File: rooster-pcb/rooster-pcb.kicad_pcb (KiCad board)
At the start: 2 copper layers, 228 x 72 mm, 95 parts, among them SW0-0 SW_Push, SW0-1 SW_Push, SW0-10 SW_Push, SW0-11 SW_Push, SW0-2 SW_Push, SW0-3 SW_Push, SW0-4 SW_Push, SW0-5 SW_Push, SW0-6 SW_Push, SW0-7 SW_Push, SW0-8 SW_Push, SW0-9 SW_Push, SW1-0 SW_Push, SW1-1 SW_Push, SW1-10 SW_Push, SW1-11 SW_Push, SW1-2 SW_Push, SW1-3 SW_Push, SW1-4 SW_Push, SW1-5 SW_Push, SW1-6 SW_Push, SW1-7 SW_Push, SW1-8 SW_Push, SW1-9 SW_Push, SW2-0 SW_Push, SW2-1 SW_Push, SW2-10 SW_Push, SW2-11 SW_Push, SW2-2 SW_Push, SW2-3 SW_Push, SW2-4 SW_Push, SW2-5 SW_Push, SW2-6 SW_Push, SW2-7 SW_Push, SW2-8 SW_Push, SW2-9 SW_Push, SW3-0 SW_Push, SW3-1 SW_Push, SW3-10 SW_Push, SW3-11 SW_Push, SW3-2 SW_Push, SW3-3 SW_Push, SW3-4 SW_Push, SW3-5 SW_Push, SW3-7 SW_Push, SW3-8 SW_Push, SW3-9 SW_Push, U1 Sparkfun_Pro_Micro

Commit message: Replaced ProMicro symbol & footprint; adding mounting holes
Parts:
- added M1: MountingHole_2.2mm_M2_Pad_Via, MountingHole:MountingHole_2.2mm_M2_Pad_Via, F.Cu at (39.5, 39.0)
- added M2: MountingHole_2.2mm_M2_Pad_Via, MountingHole:MountingHole_2.2mm_M2_Pad_Via, F.Cu at (39.5, 75.0)
- added REF**: MountingHole_2.2mm_M2_Pad_Via, MountingHole:MountingHole_2.2mm_M2_Pad_Via, F.Cu at (229.5, 39.0)
- added REF**: MountingHole_2.2mm_M2_Pad_Via, MountingHole:MountingHole_2.2mm_M2_Pad_Via, F.Cu at (229.5, 75.0)
- U1: value Sparkfun_Pro_Micro -> ProMicro; footprint Arduino:Sparkfun_Pro_Micro -> Keyboard_Components:ArduinoProMicro
- moved U1 32.5 mm to (68.0, 40.2), turned to 270 degrees
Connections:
- SW0-10 pad 2: COLA -> COL10
- SW0-11 pad 2: COLB -> COL11
- SW1-10 pad 2: COLA -> COL10
- SW1-11 pad 2: COLB -> COL11
- SW2-10 pad 2: COLA -> COL10
- SW2-11 pad 2: COLB -> COL11
- SW3-10 pad 2: COLA -> COL10
- SW3-11 pad 2: COLB -> COL11
- U1 pad 1: COL1 -> Net-(U1-Pad1)
- U1 pad 10: COL7 -> ROW1
- U1 pad 11: COL8 -> ROW2
- U1 pad 12: COL9 -> ROW3
- U1 pad 13: COLA -> COL4
- U1 pad 14: COLB -> COL5
- U1 pad 15: ROW0 -> COL6
- U1 pad 16: ROW1 -> COL7
- U1 pad 17: ROW2 -> COL8
- U1 pad 18: ROW3 -> COL9
- U1 pad 19: Net-(U1-Pad19) -> COL10
- U1 pad 2: COL0 -> Net-(U1-Pad2)
- U1 pad 20: Net-(U1-Pad20) -> COL11
- U1 pad 5: COL2 -> COL0
- U1 pad 6: COL3 -> COL1
- U1 pad 7: COL4 -> COL2
- U1 pad 8: COL5 -> COL3
- U1 pad 9: COL6 -> ROW0

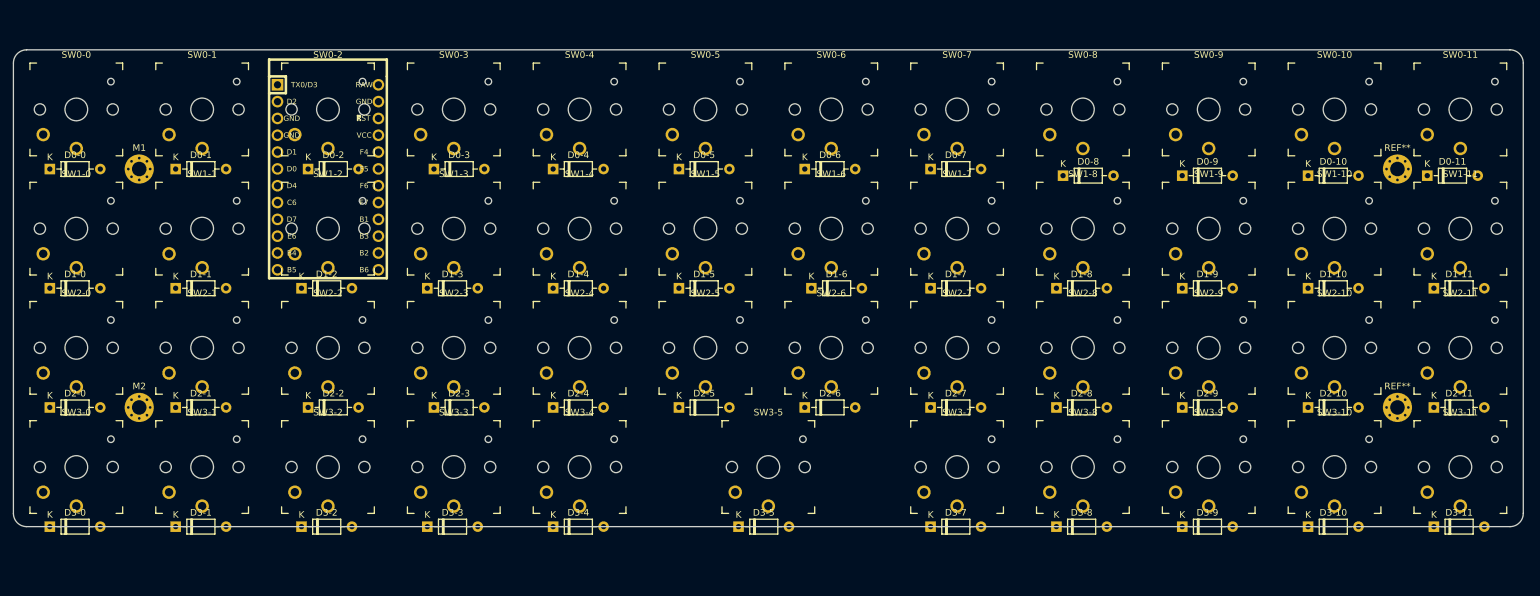
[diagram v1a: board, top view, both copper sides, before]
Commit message: Positioned diodes
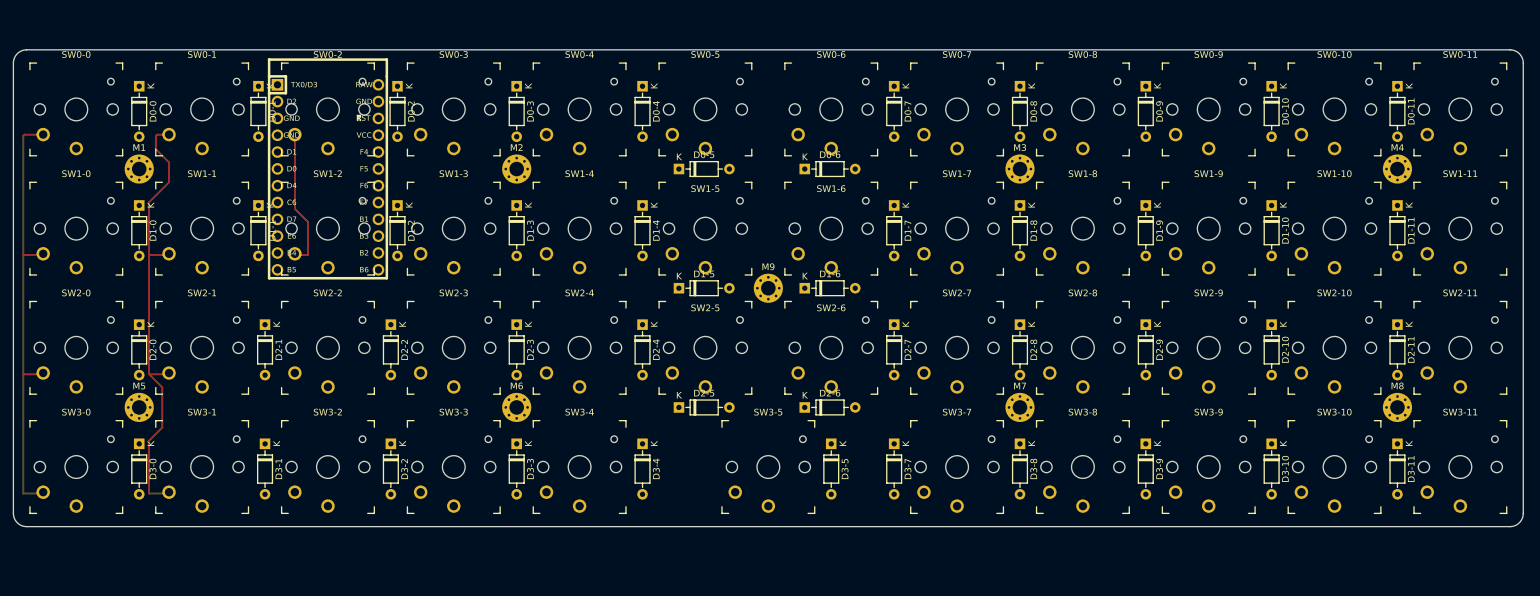
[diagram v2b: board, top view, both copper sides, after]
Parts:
- added M2: MountingHole_2.2mm_M2_Pad_Via, MountingHole:MountingHole_2.2mm_M2_Pad_Via, F.Cu at (96.5, 39.0)
- added M3: MountingHole_2.2mm_M2_Pad_Via, MountingHole:MountingHole_2.2mm_M2_Pad_Via, F.Cu at (172.5, 39.0)
- added M6: MountingHole_2.2mm_M2_Pad_Via, MountingHole:MountingHole_2.2mm_M2_Pad_Via, F.Cu at (96.5, 75.0)
- added M7: MountingHole_2.2mm_M2_Pad_Via, MountingHole:MountingHole_2.2mm_M2_Pad_Via, F.Cu at (172.5, 75.0)
- added M9: MountingHole_2.2mm_M2_Pad_Via, MountingHole:MountingHole_2.2mm_M2_Pad_Via, F.Cu at (134.5, 57.0)
- moved D1-2 19.1 mm to (78.5, 44.5), turned to 270 degrees
- moved D3-5 18.8 mm to (144.0, 80.5), turned to 270 degrees
- moved D0-0 18.4 mm to (39.5, 26.5), turned to 270 degrees
- moved D0-2 18.4 mm to (78.5, 26.5), turned to 270 degrees
- moved D0-4 18.4 mm to (115.5, 26.5), turned to 270 degrees
- moved D1-0 18.4 mm to (39.5, 44.5), turned to 270 degrees
- moved D1-3 18.4 mm to (96.5, 44.5), turned to 270 degrees
- moved D1-4 18.4 mm to (115.5, 44.5), turned to 270 degrees
- moved D2-0 18.4 mm to (39.5, 62.5), turned to 270 degrees
- moved D2-1 18.4 mm to (58.5, 62.5), turned to 270 degrees
- moved D2-4 18.4 mm to (115.5, 62.5), turned to 270 degrees
- moved D3-0 18.4 mm to (39.5, 80.5), turned to 270 degrees
- moved D3-1 18.4 mm to (58.5, 80.5), turned to 270 degrees
- moved D3-2 18.4 mm to (77.5, 80.5), turned to 270 degrees
- moved D3-3 18.4 mm to (96.5, 80.5), turned to 270 degrees
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- renumbered REF** to M4, M2 to M5, REF** to M8
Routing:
- net COL1: track 0.00 -> 69.1 mm
- net COL0: track 0.00 -> 66.3 mm
- net COL2: track 0.00 -> 21.1 mm

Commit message: Flipped diodes to back side; started tracing columns
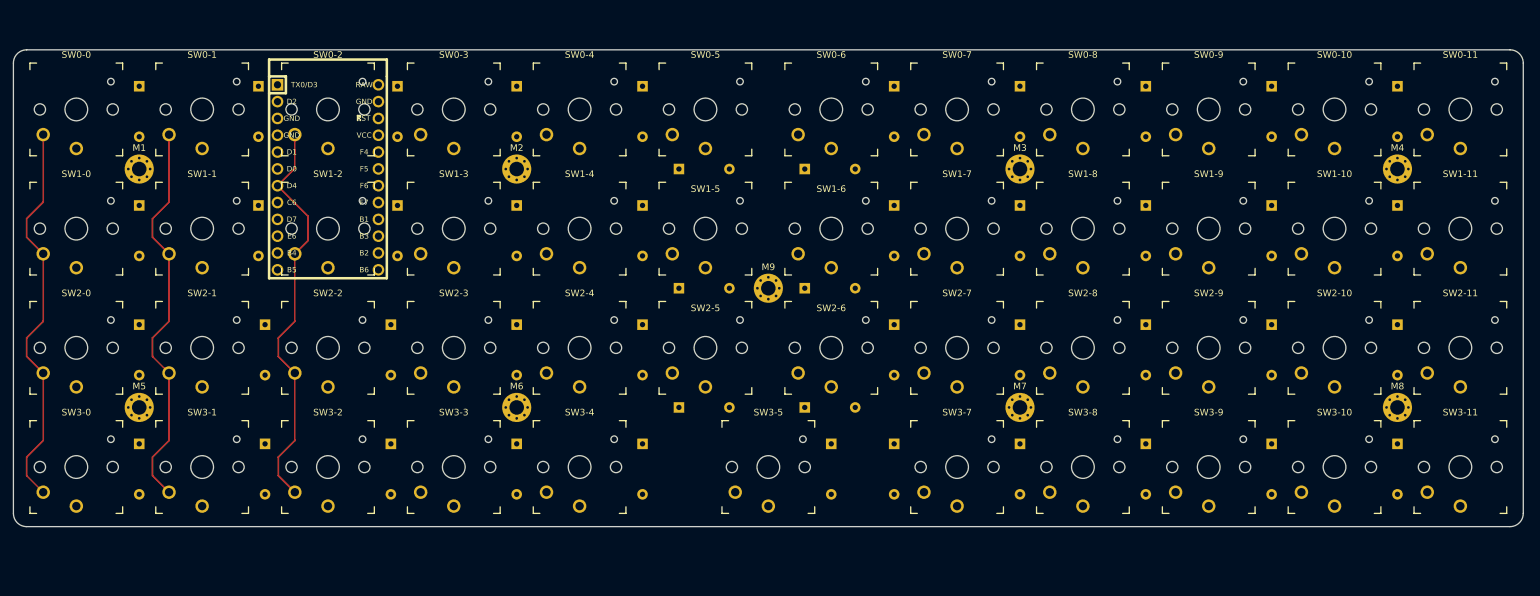
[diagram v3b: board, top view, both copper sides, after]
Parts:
- D0-0, D0-1, D0-10, D0-11, D0-2, D0-3, D0-4, D0-5, D0-6, D0-7, D0-8, D0-9, D1-0, D1-1, D1-10, D1-11, D1-2, D1-3, D1-4, D1-5, D1-6, D1-7, D1-8, D1-9, D2-0, D2-1, D2-10, D2-11, D2-2, D2-3, D2-4, D2-5, D2-6, D2-7, D2-8, D2-9, D3-0, D3-1, D3-10, D3-11, D3-2, D3-3, D3-4, D3-5, D3-7, D3-8, D3-9: moved to B.Cu
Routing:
- net COL2: track 21.1 -> 62.3 mm
- net COL1: track 69.1 -> 61.1 mm
- net COL0: track 66.3 -> 61.1 mm

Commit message: Adding horizontal traces
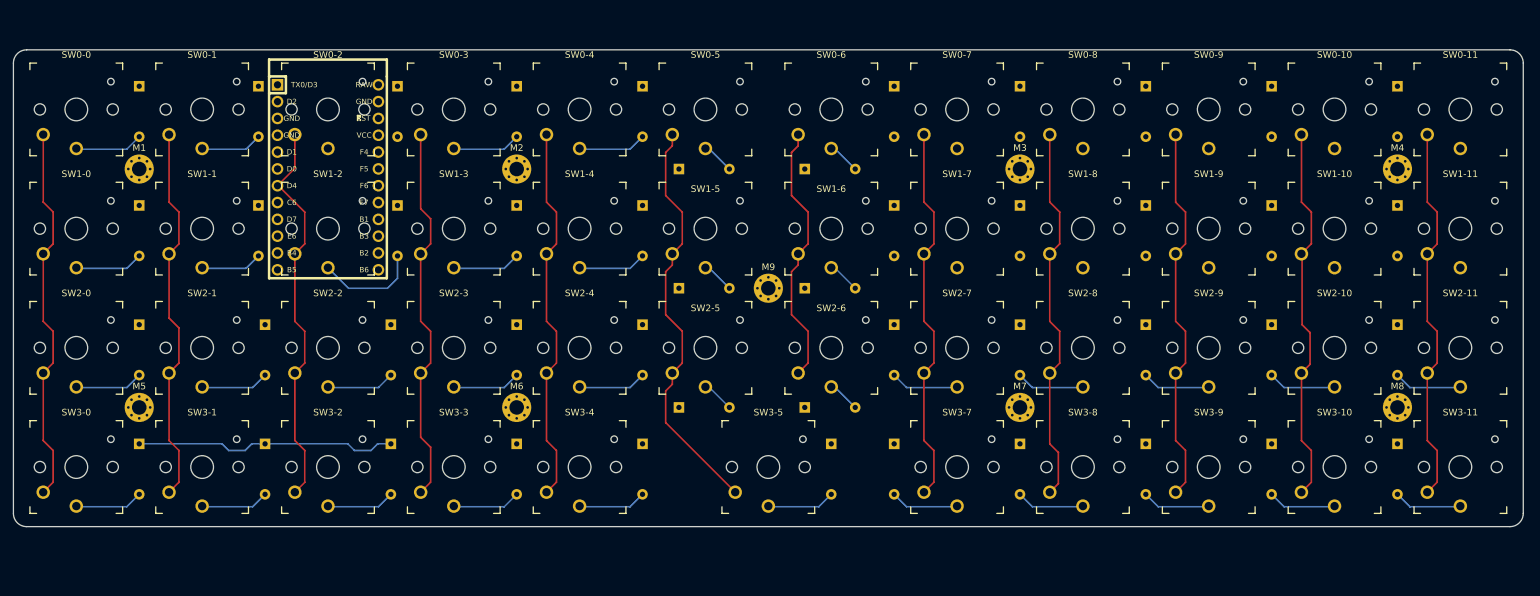
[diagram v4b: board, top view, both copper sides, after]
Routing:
- net COL5: track 0.00 -> 62.9 mm
- net COL9: track 0.00 -> 57.7 mm
- net COL7: track 0.00 -> 57.7 mm
- net COL4: track 0.00 -> 57.7 mm
- net COL3: track 0.00 -> 57.7 mm
- net COL11: track 0.00 -> 57.7 mm
- net COL8: track 0.00 -> 57.6 mm
- net COL10: track 0.00 -> 57.6 mm
- net COL6: track 0.00 -> 40.1 mm
- net ROW3: track 0.00 -> 39.7 mm
- net Net-(D1-2-Pad2): track 0.00 -> 15.8 mm
- net Net-(D1-4-Pad2): track 0.00 -> 10.3 mm
- net Net-(D1-3-Pad2): track 0.00 -> 10.3 mm
- net Net-(D0-4-Pad2): track 0.00 -> 10.3 mm
- net Net-(D0-3-Pad2): track 0.00 -> 10.3 mm
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
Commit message: Finished routing; design rules passed
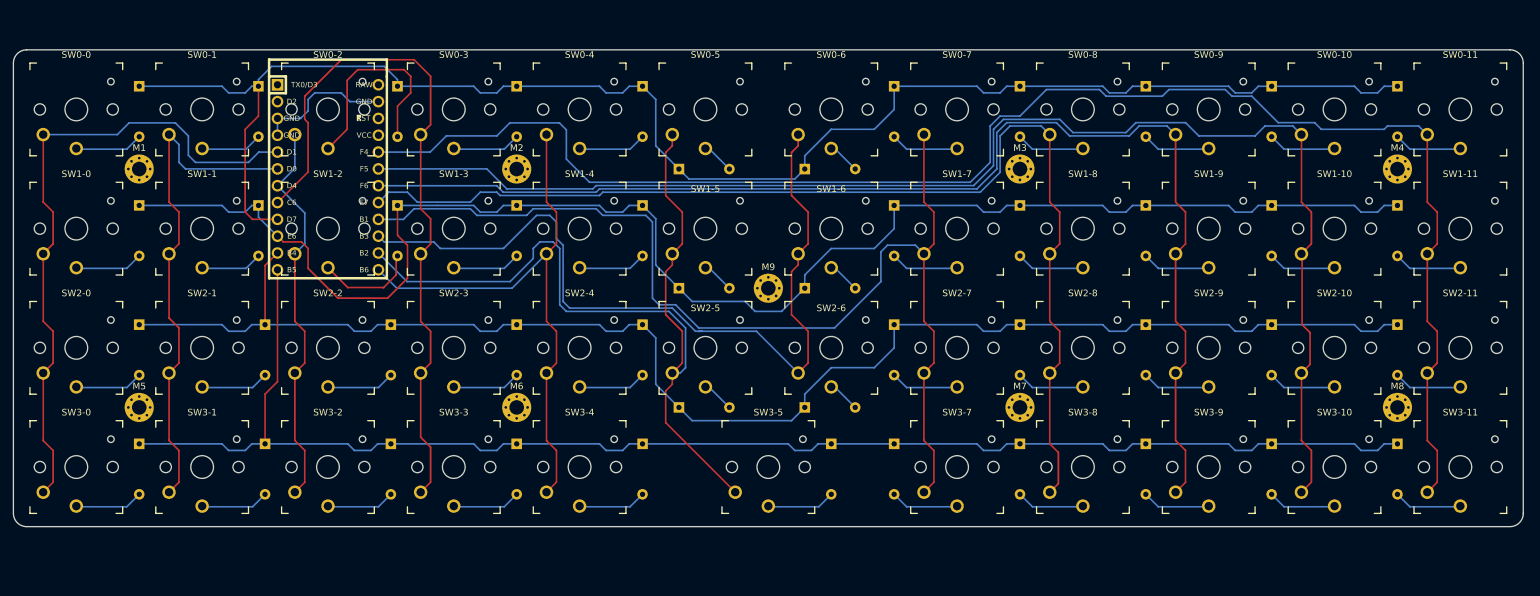
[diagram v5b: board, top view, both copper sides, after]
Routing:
- net ROW0: track 0.00 -> 244.5 mm
- net ROW1: track 0.00 -> 239.3 mm
- net ROW2: track 0.00 -> 227.6 mm
- net ROW3: track 39.7 -> 224.5 mm
- net COL11: track 57.7 -> 237.3 mm
- net COL10: track 57.6 -> 209.2 mm
- net COL9: track 57.7 -> 188.1 mm
- net COL8: track 57.6 -> 169.1 mm
- net COL7: track 57.7 -> 164.1 mm
- net COL6: track 40.1 -> 123.3 mm
- net COL5: track 62.9 -> 133.1 mm
- net COL3: track 57.7 -> 107.6 mm
- net COL0: track 58.6 -> 99.5 mm
- net Net-(D0-2-Pad2): track 0.00 -> 32.1 mm
- net COL4: track 57.7 -> 86.4 mm
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
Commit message: Remade PCB for 0.5mm spacing between keycaps + surface-mounted diodes
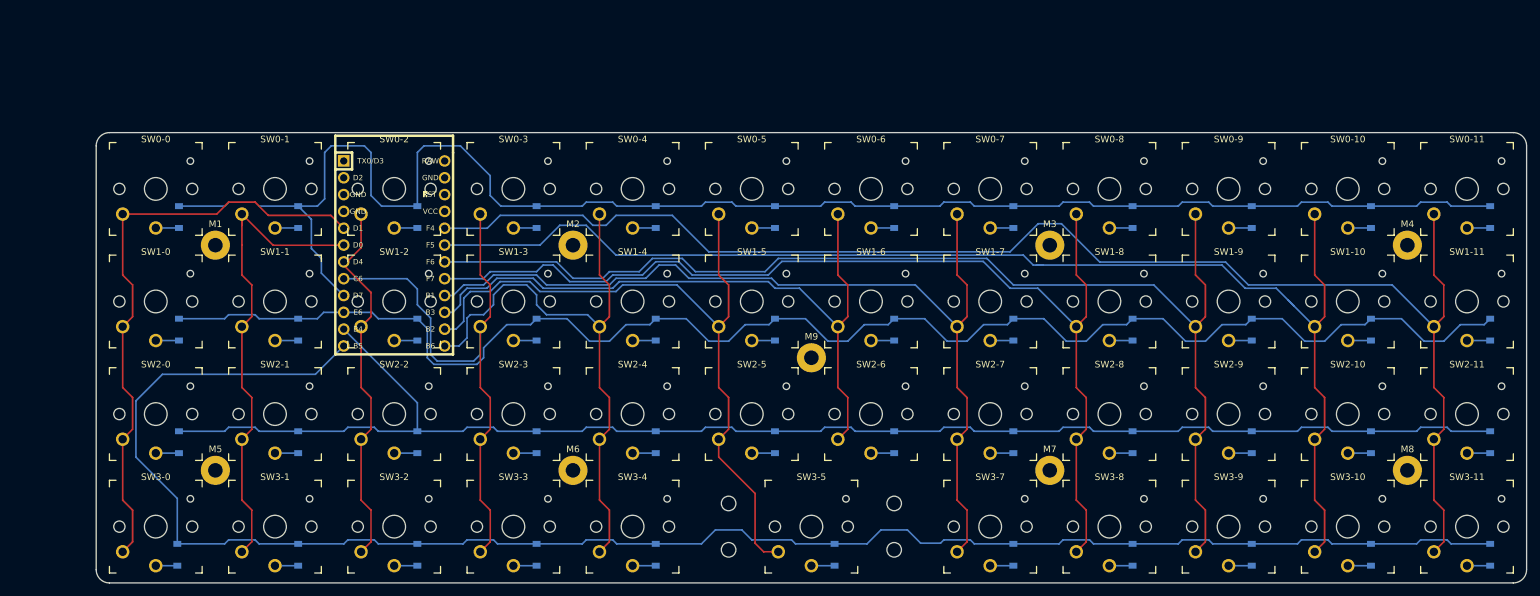
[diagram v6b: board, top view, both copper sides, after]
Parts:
- added N1: MountingHole_2.2mm_M2, MountingHole:MountingHole_2.2mm_M2, F.Cu at (128.5, 89.5)
- added N2: MountingHole_2.2mm_M2, MountingHole:MountingHole_2.2mm_M2, F.Cu at (153.5, 89.5)
- added N3: MountingHole_2.2mm_M2, MountingHole:MountingHole_2.2mm_M2, F.Cu at (128.5, 96.5)
- added N4: MountingHole_2.2mm_M2, MountingHole:MountingHole_2.2mm_M2, F.Cu at (153.5, 96.5)
- D0-0, D0-1, D0-10, D0-11, D0-2, D0-3, D0-4, D0-5, D0-6, D0-7, D0-8, D0-9, D1-0, D1-1, D1-10, D1-11, D1-2, D1-3, D1-4, D1-5, D1-6, D1-7, D1-8, D1-9, D2-0, D2-1, D2-10, D2-11, D2-2, D2-3, D2-4, D2-5, D2-6, D2-7, D2-8, D2-9, D3-0, D3-1, D3-10, D3-11, D3-2, D3-3, D3-4, D3-5, D3-7, D3-8, D3-9: footprint Diode_THT:D_DO-35_SOD27_P7.62mm_Horizontal -> Diode_SMD:D_SOD-123
- M1, M2, M3, M4, M5, M6, M7, M8, M9: value MountingHole_2.2mm_M2_Pad_Via -> MountingHole_2.2mm_M2_Pad; footprint MountingHole:MountingHole_2.2mm_M2_Pad_Via -> MountingHole:MountingHole_2.2mm_M2_Pad
- moved D0-7 26.7 mm to (171.5, 46.2)
- moved D0-8 26.1 mm to (189.5, 46.2)
- moved D1-7 26.0 mm to (171.5, 63.2)
- moved D0-9 25.4 mm to (207.5, 46.2)
- moved D1-8 25.3 mm to (189.5, 63.2)
- moved D2-7 25.3 mm to (171.5, 80.2)
- moved D0-10 24.8 mm to (225.5, 46.2)
- moved D1-9 24.6 mm to (207.5, 63.2)
- moved D3-7 24.6 mm to (171.5, 97.2)
- moved D2-8 24.6 mm to (189.5, 80.2)
- moved D0-11 24.2 mm to (243.5, 46.2)
- moved D1-10 24.0 mm to (225.5, 63.2)
- moved D2-9 23.9 mm to (207.5, 80.2)
- moved D3-8 23.9 mm to (189.5, 97.2)
- moved D1-11 23.4 mm to (243.5, 63.2)
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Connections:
- U1 pad 3: GND -> Net-(U1-Pad3)
- U1 pad 4: GND -> Net-(U1-Pad4)
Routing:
- net ROW3: track 224.5 -> 265.1 mm
- net Net-(D0-2-Pad2): track 32.1 -> 3.50 mm
- net COL7: track 164.1 -> 139.1 mm
- net COL5: track 133.1 -> 108.6 mm
- net GND: track 20.9 -> 0.00 mm
- net COL11: track 237.3 -> 216.6 mm
- net COL6: track 123.3 -> 102.7 mm
- net COL3: track 107.6 -> 89.7 mm
- net COL10: track 209.2 -> 195.9 mm
- net Net-(D1-2-Pad2): track 15.3 -> 3.50 mm
- net COL9: track 188.1 -> 176.3 mm
- net COL8: track 169.1 -> 159.0 mm
- net COL0: track 99.5 -> 90.5 mm
- net ROW1: track 239.3 -> 231.0 mm
- net Net-(D3-0-Pad2): track 10.3 -> 3.25 mm
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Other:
- board size 228 x 72 mm -> 216 x 68 mm
